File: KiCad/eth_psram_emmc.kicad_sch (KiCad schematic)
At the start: 39 parts, among them IC5 MX52LM04A11XVW, IC6 LAN8742A-CZ-TR, IC7 APS256XXN-OBR-BG, Y2 VXM7-9032-25M0000000

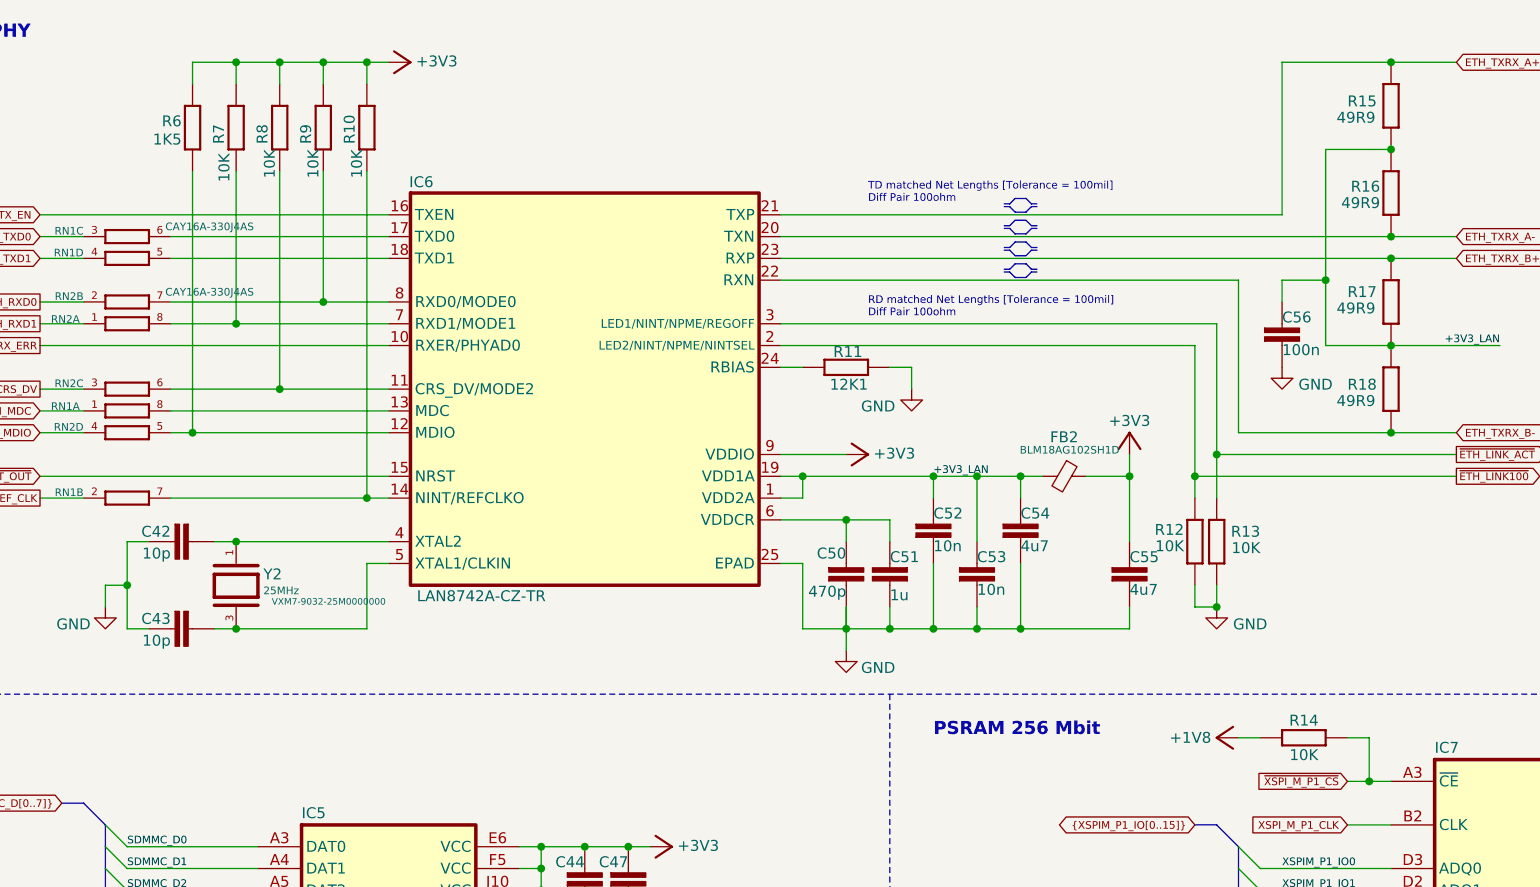
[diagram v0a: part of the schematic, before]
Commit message: Removed all blind/burned vias
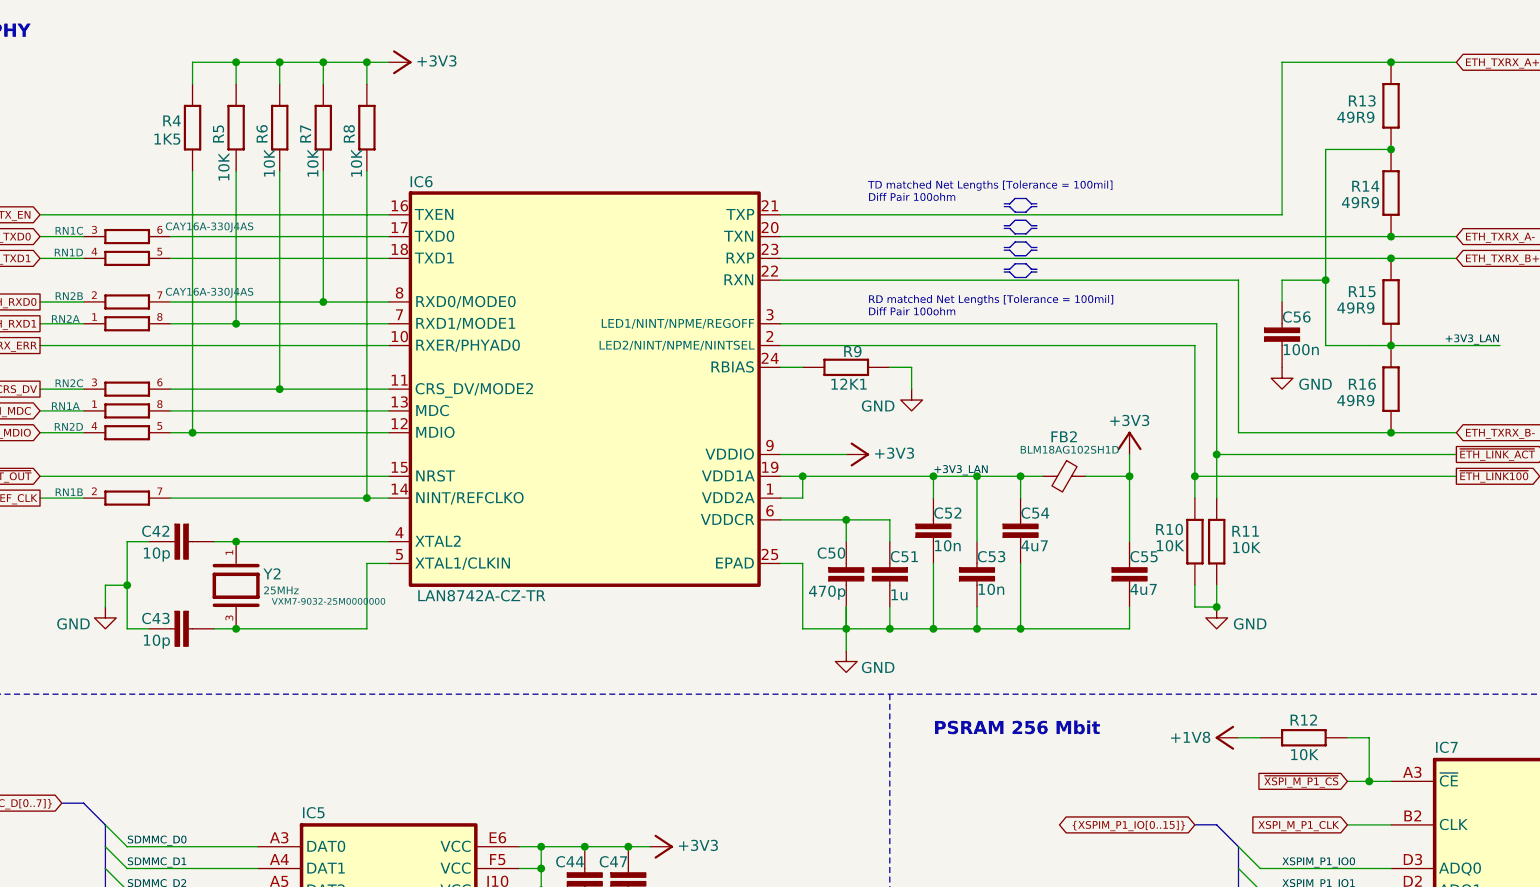
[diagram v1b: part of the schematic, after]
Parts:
- C42, C43: footprint PCM_EEZ_passives:C_0603_1608Metric -> PCM_EEZ_passives:C_0402_1005Metric; DigiKey 1276-1069-1-ND -> (none); LCSC C318677 -> (none); Mouser 187-CL10C100CB8NNNC -> (none); TME VJ0603A100JXACW1BC -> (none)
- renumbered R12 to R10, R13 to R11, R14 to R12, R15 to R13, R16 to R14, R17 to R15, R18 to R16, R6 to R4, R7 to R5, R8 to R6, R9 to R7, R10 to R8, R11 to R9
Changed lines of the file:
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@@
 		(on_board yes)
 		(dnp no)
-		(property "Reference" "R11"
+		(property "Reference" "R9"
 			(at 136.525 53.34 90)
 			(effects
@@
 			(project "BB3plus CM5 STM32H7 module"
 				(path "/1a4f0aea-3a69-423f-8790-3103cd0321c4/db533ab3-e8cc-4dba-934e-bd27ee1dfc29"
-					(reference "R11")
+					(reference "R9")
 					(unit 1)
 				)
@@
 		(on_board yes)
 		(dnp no)
-		(property "Reference" "R7"
+		(property "Reference" "R5"
 			(at 62.23 29.845 90)
 			(effects
@@
 			(project "BB3plus CM5 STM32H7 module"
 				(path "/1a4f0aea-3a69-423f-8790-3103cd0321c4/db533ab3-e8cc-4dba-934e-bd27ee1dfc29"
-					(reference "R7")
+					(reference "R5")
 					(unit 1)
 				)
@@
 		(on_board yes)
 		(dnp no)
-		(property "Reference" "R15"
+		(property "Reference" "R13"
 			(at 193.04 24.13 0)
 			(effects
@@
 			(project "BB3plus CM5 STM32H7 module"
 				(path "/1a4f0aea-3a69-423f-8790-3103cd0321c4/db533ab3-e8cc-4dba-934e-bd27ee1dfc29"
-					(reference "R15")
+					(reference "R13")
 					(unit 1)
 				)
@@
 		(on_board yes)
 		(dnp no)
-		(property "Reference" "R8"
+		(property "Reference" "R6"
 			(at 67.31 29.845 90)
 			(effects
@@
 			(project "BB3plus CM5 STM32H7 module"
 				(path "/1a4f0aea-3a69-423f-8790-3103cd0321c4/db533ab3-e8cc-4dba-934e-bd27ee1dfc29"
-					(reference "R8")
+					(reference "R6")
 					(unit 1)
 				)
@@
 		(on_board yes)
 		(dnp no)
-		(property "Reference" "R18"
+		(property "Reference" "R16"
 			(at 193.04 57.15 0)
 			(effects
@@
 			(project "BB3plus CM5 STM32H7 module"
 				(path "/1a4f0aea-3a69-423f-8790-3103cd0321c4/db533ab3-e8cc-4dba-934e-bd27ee1dfc29"
-					(reference "R18")
+					(reference "R16")
 					(unit 1)
 				)
@@
 		(on_board yes)
 		(dnp no)
-		(property "Reference" "R12"
+		(property "Reference" "R10"
 			(at 173.99 75.565 0)
 			(effects
@@
 			(project "BB3plus CM5 STM32H7 module"
 				(path "/1a4f0aea-3a69-423f-8790-3103cd0321c4/db533ab3-e8cc-4dba-934e-bd27ee1dfc29"
-					(reference "R12")
+					(reference "R10")
 					(unit 1)
 				)
@@
 		(on_board yes)
 		(dnp no)
-		(property "Reference" "R6"
+		(property "Reference" "R4"
 			(at 57.15 27.94 0)
 			(effects
@@
 			(project "BB3plus CM5 STM32H7 module"
 				(path "/1a4f0aea-3a69-423f-8790-3103cd0321c4/db533ab3-e8cc-4dba-934e-bd27ee1dfc29"
-					(reference "R6")
+					(reference "R4")
 					(unit 1)
 				)
@@
 		(on_board yes)
 		(dnp no)
-		(property "Reference" "R13"
+		(property "Reference" "R11"
 			(at 182.88 74.295 0)
 			(effects
@@
 			(project "BB3plus CM5 STM32H7 module"
 				(path "/1a4f0aea-3a69-423f-8790-3103cd0321c4/db533ab3-e8cc-4dba-934e-bd27ee1dfc29"
-					(reference "R13")
+					(reference "R11")
 					(unit 1)
 				)
@@
 		(on_board yes)
 		(dnp no)
-		(property "Reference" "R16"
+		(property "Reference" "R14"
 			(at 196.85 35.56 0)
 			(effects
@@
 			(project "BB3plus CM5 STM32H7 module"
 				(path "/1a4f0aea-3a69-423f-8790-3103cd0321c4/db533ab3-e8cc-4dba-934e-bd27ee1dfc29"
-					(reference "R16")
+					(reference "R14")
 					(unit 1)
 				)
@@
 		(on_board yes)
 		(dnp no)
-		(property "Reference" "R14"
+		(property "Reference" "R12"
 			(at 187.96 97.79 90)
 			(effects
@@
 			(project "BB3plus CM5 STM32H7 module"
 				(path "/1a4f0aea-3a69-423f-8790-3103cd0321c4/db533ab3-e8cc-4dba-934e-bd27ee1dfc29"
-					(reference "R14")
+					(reference "R12")
 					(unit 1)
 				)
@@
 		(on_board yes)
 		(dnp no)
-		(property "Reference" "R17"
+		(property "Reference" "R15"
 			(at 193.04 46.355 0)
 			(effects
@@
 			(project "BB3plus CM5 STM32H7 module"
 				(path "/1a4f0aea-3a69-423f-8790-3103cd0321c4/db533ab3-e8cc-4dba-934e-bd27ee1dfc29"
-					(reference "R17")
+					(reference "R15")
 					(unit 1)
 				)
@@
 			)
 		)
-		(property "Footprint" "PCM_EEZ_passives:C_0603_1608Metric"
+		(property "Footprint" "PCM_EEZ_passives:C_0402_1005Metric"
 			(at 53.34 76.2 0)
 			(effects
@@
 			)
 		)
-		(property "TME" "VJ0603A100JXACW1BC"
+		(property "TME" ""
 			(at 55.88 76.2 0)
 			(effects
@@
 			)
 		)
-		(property "DigiKey" "1276-1069-1-ND"
+		(property "DigiKey" ""
 			(at 55.88 76.2 0)
 			(effects
@@
 			)
 		)
-		(property "Mouser" "187-CL10C100CB8NNNC"
+		(property "Mouser" ""
 			(at 55.88 76.2 0)
 			(effects
@@
 			)
 		)
-		(property "LCSC" "C318677"
+		(property "LCSC" ""
 			(at 55.88 76.2 0)
 			(effects
@@
 			)
 		)
-		(property "Footprint" "PCM_EEZ_passives:C_0603_1608Metric"
+		(property "Footprint" "PCM_EEZ_passives:C_0402_1005Metric"
 			(at 53.34 86.36 0)
 			(effects
@@
 			)
 		)
-		(property "TME" "VJ0603A100JXACW1BC"
+		(property "TME" ""
 			(at 55.88 86.36 0)
 			(effects
@@
 			)
 		)
-		(property "DigiKey" "1276-1069-1-ND"
+		(property "DigiKey" ""
 			(at 55.88 86.36 0)
 			(effects
@@
 			)
 		)
-		(property "Mouser" "187-CL10C100CB8NNNC"
+		(property "Mouser" ""
 			(at 55.88 86.36 0)
 			(effects
@@
 			)
 		)
-		(property "LCSC" "C318677"
+		(property "LCSC" ""
 			(at 55.88 86.36 0)
 			(effects
@@
 		(on_board yes)
 		(dnp no)
-		(property "Reference" "R9"
+		(property "Reference" "R7"
 			(at 72.39 29.845 90)
 			(effects
@@
 			(project "BB3plus CM5 STM32H7 module"
 				(path "/1a4f0aea-3a69-423f-8790-3103cd0321c4/db533ab3-e8cc-4dba-934e-bd27ee1dfc29"
-					(reference "R9")
+					(reference "R7")
 					(unit 1)
 				)
@@
 		(on_board yes)
 		(dnp no)
-		(property "Reference" "R10"
+		(property "Reference" "R8"
 			(at 77.47 29.845 90)
 			(effects
@@
 			(project "BB3plus CM5 STM32H7 module"
 				(path "/1a4f0aea-3a69-423f-8790-3103cd0321c4/db533ab3-e8cc-4dba-934e-bd27ee1dfc29"
-					(reference "R10")
+					(reference "R8")
 					(unit 1)
 				)
